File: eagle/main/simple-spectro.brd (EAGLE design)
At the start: 99.1 x 73.7 mm, 46 parts, among them CON1 BAT, CON2 SPI, CON3 SPI, IC1 32U4, IC2 MCP73831T, IC3 MCP1703-33, IC4 DMP1045U, X1 8MHz, X2 MINI-USB

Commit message: add files for new price offer with assembly
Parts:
- C4, C5: value 10µF -> 10u
- R3: value 10K\ -> 10K

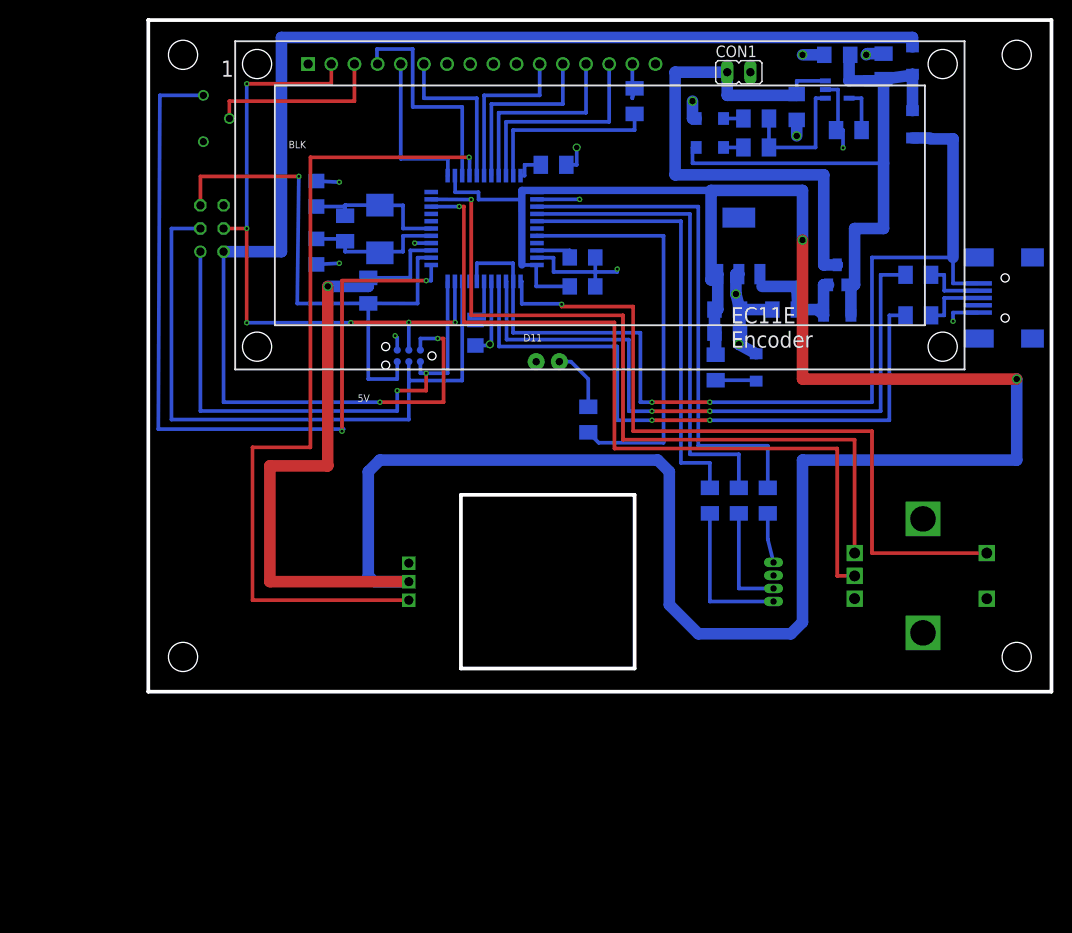
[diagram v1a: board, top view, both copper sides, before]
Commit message: remove right angles
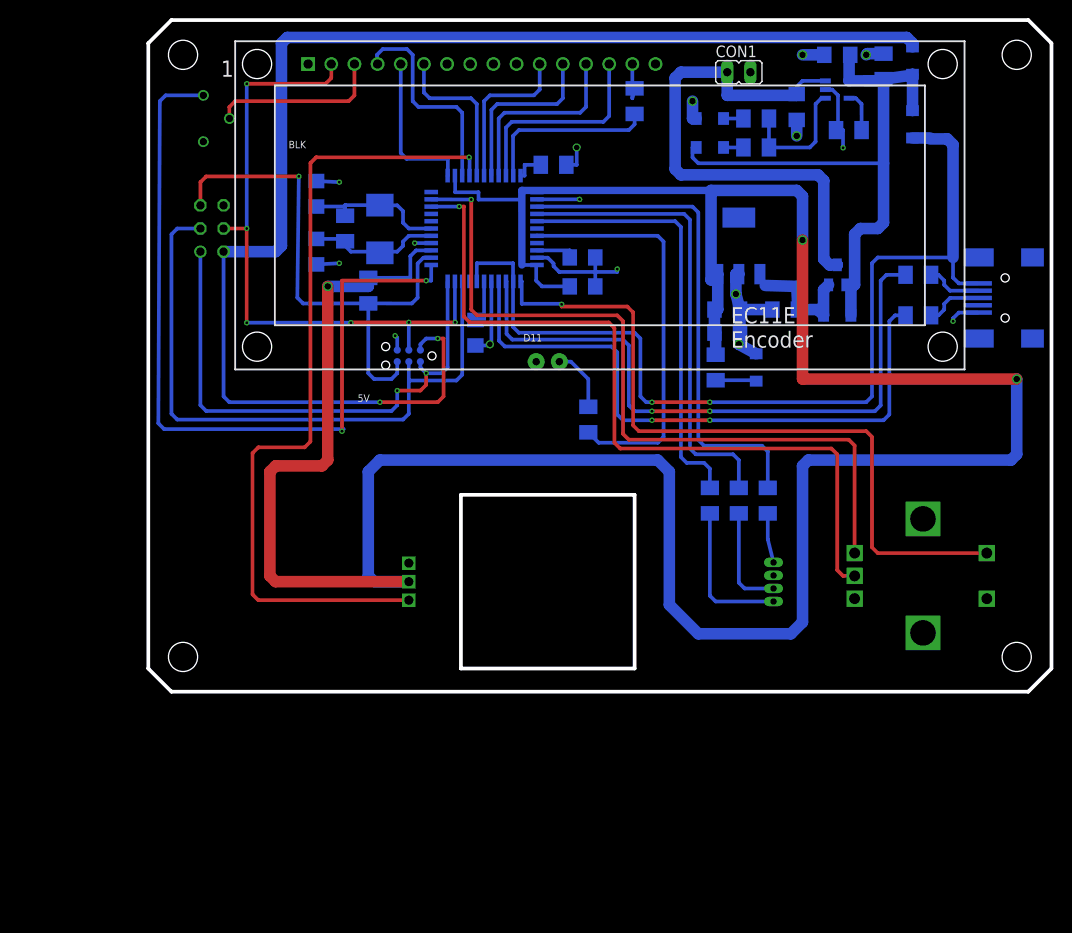
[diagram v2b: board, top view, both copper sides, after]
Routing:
- net VCC: track 332.0 -> 329.0 mm
- net VUSB: track 108.5 -> 105.9 mm
- net RESET: track 61.0 -> 58.8 mm
- net ISP+5V: track 151.5 -> 149.3 mm
- net USB_N: track 73.0 -> 71.2 mm
- net RX: track 87.0 -> 85.1 mm
- net MISO: track 60.7 -> 58.9 mm
- net GND: track 91.9 -> 90.0 mm
- net VBAT1: track 59.7 -> 57.8 mm
- net USB_P: track 71.4 -> 69.5 mm
- net D7*: track 81.2 -> 79.7 mm
- net TX: track 85.2 -> 83.7 mm
- net SCK: track 73.2 -> 71.8 mm
- net A6: track 24.9 -> 23.5 mm
- net D12*: track 91.5 -> 90.1 mm
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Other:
- outline, holes or cut-outs redrawn

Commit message: towards final box
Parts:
- moved R5 1.27 mm to (84.5, 44.5)
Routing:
- net USB_N: track 71.2 -> 69.9 mm
- net USBC_N: track 6.12 -> 5.28 mm

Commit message: update bom
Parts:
- D1, D2, D3: device lpatiny:LED-1206 -> diode:SOD123
- IC4: value DMP1045U -> DMP1045U or DMG2302
- moved D3 0.63 mm to (75.6, 41.9), turned to 180 degrees
- turned D1 to 270 degrees
- turned D2 to 90 degrees
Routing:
- net N$11: track 4.87 -> 2.77 mm
- net VDD: track 14.7 -> 13.4 mm
- net N$15: track 67.9 -> 66.7 mm

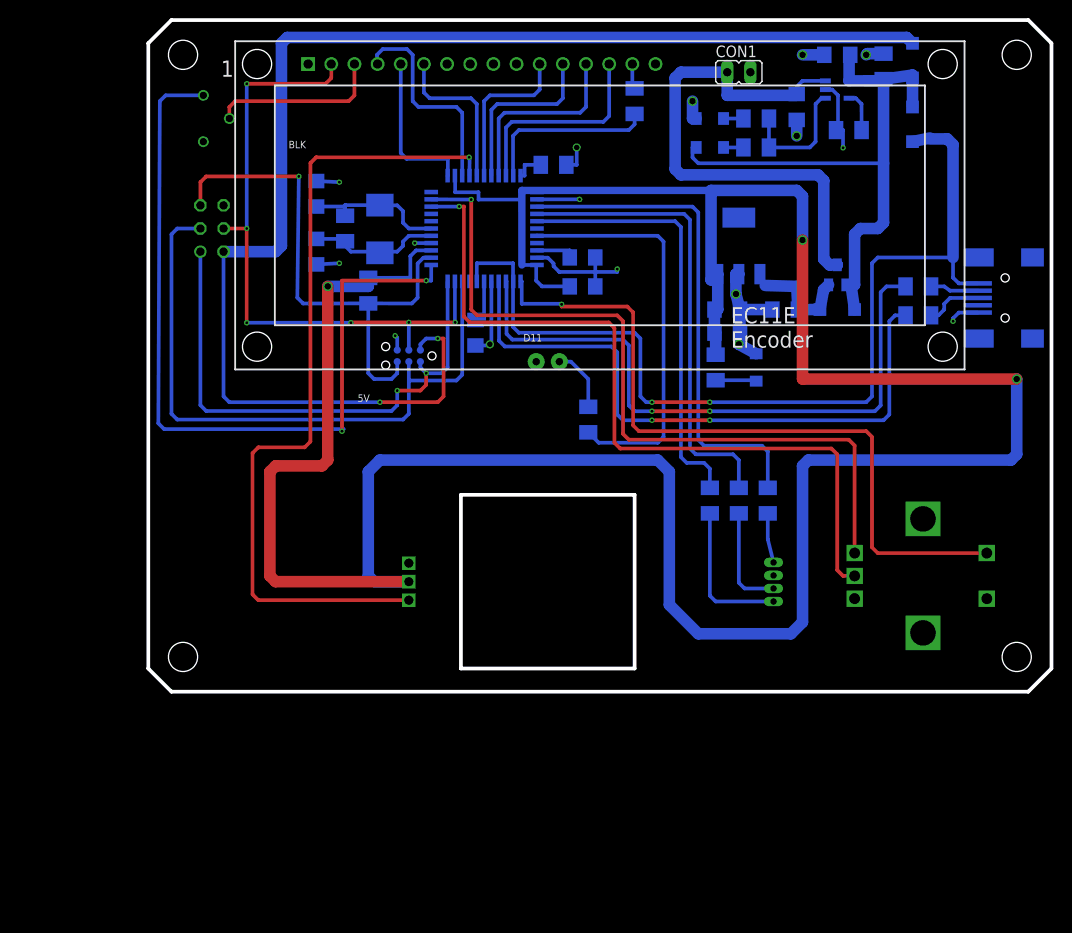
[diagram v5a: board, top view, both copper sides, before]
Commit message: add i2c temperature sensor
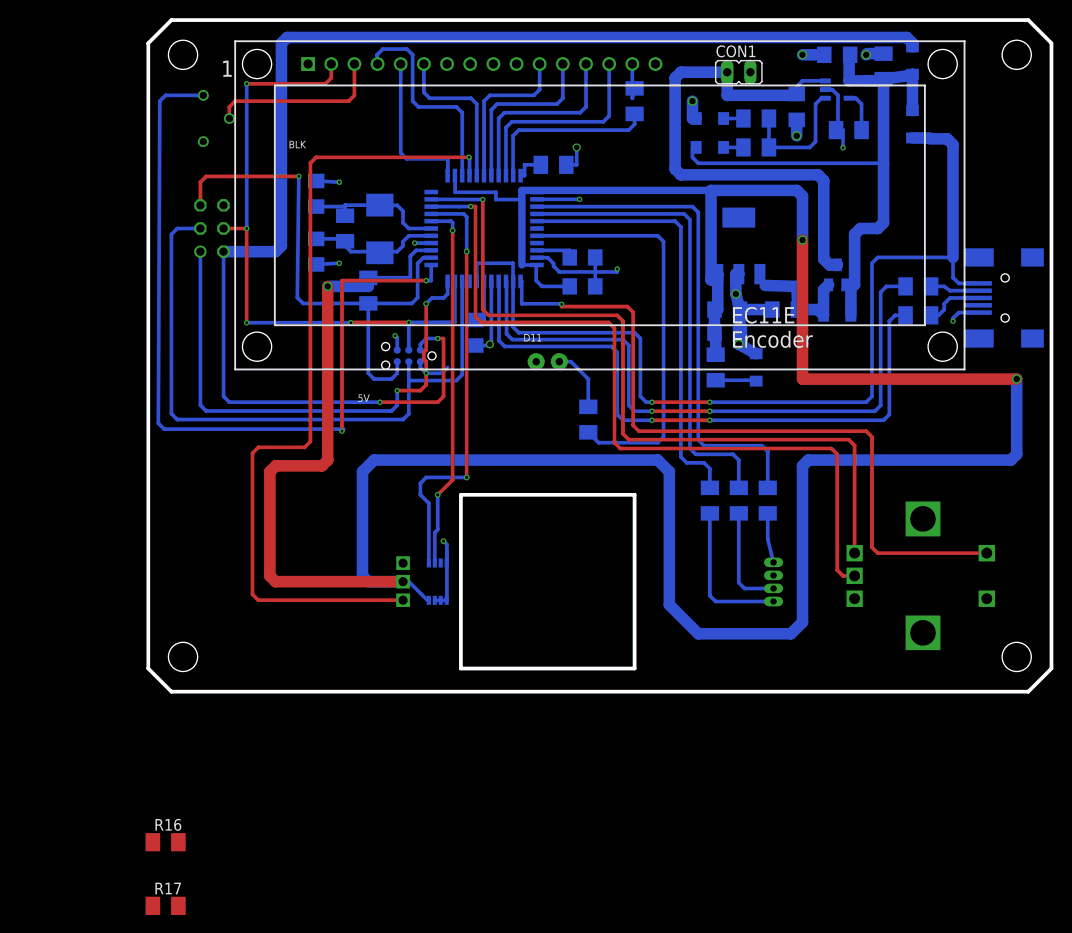
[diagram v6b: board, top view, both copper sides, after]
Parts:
- added R16, R17: 10K, rcl:M1206
- added U1: TMP75DGK, ti_tmp:MSOP8
- D1, D2, D3: device diode:SOD123 -> lpatiny:LED-1206
- IC4: value DMP1045U or DMG2302 -> DMP1045U
- moved U$7 0.64 mm to (25.4, 12.1)
- moved D3 0.63 mm to (75.6, 41.3), turned to 0 degrees
- turned D1 to 90 degrees
- turned D2 to 270 degrees
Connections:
- net GND: now also U1.4, U1.5, U1.6, U1.7
- net SCL: now also R17.1, U1.2
- net SDA: now also R16.1, U1.1
- net VCC: now also R16.2, R17.2, U1.8
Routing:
- net SDA: track 0.00 -> 47.1 mm, vias 0 -> 2
- net SCL: track 0.00 -> 40.6 mm, vias 0 -> 2
- net GND: track 90.0 -> 99.1 mm, vias 16 -> 17
- net VCC: track 329.0 -> 332.7 mm
- net MISO: track 58.9 -> 61.4 mm, vias 2 -> 3
- net N$11: track 2.77 -> 4.87 mm
- net VDD: track 13.4 -> 14.7 mm
- net N$15: track 66.7 -> 67.9 mm
- net D12*: track 90.1 -> 89.4 mm
- net MOSI: track 70.3 -> 70.2 mm, vias 6 -> 5

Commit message: clean up
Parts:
- added R18, R19: 10K, rcl:M1206
- D1, D2, D3: device lpatiny:LED-1206 -> diode:SOD123
- IC4: value DMP1045U -> DMP1045U or DMG2302
- moved R17 52.6 mm to (27.9, 22.2), flipped to the bottom
- moved R16 43.6 mm to (27.9, 18.4), flipped to the bottom
- moved U$7 0.64 mm to (26.0, 12.1)
- moved D3 0.63 mm to (75.6, 41.9), turned to 180 degrees
- turned D1 to 270 degrees
- turned D2 to 90 degrees
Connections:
- net A3: now also R18.1, R19.2
- net GND: now also R19.1
- net VBAT1: now also R18.2
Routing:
- net A3: track 0.00 -> 20.1 mm, vias 0 -> 2
- net GND: track 99.1 -> 93.9 mm, vias 17 -> 16
- net VBAT1: track 57.8 -> 61.1 mm
- net SDA: track 47.1 -> 44.4 mm, vias 2 -> 1
- net SCL: track 40.6 -> 43.0 mm
- net N$11: track 4.87 -> 2.77 mm
- net VDD: track 14.7 -> 13.4 mm
- net N$15: track 67.9 -> 66.7 mm
- net VCC: track 332.7 -> 333.9 mm
- net MISO: track 61.4 -> 62.4 mm, vias 3 -> 2
- net D12*: track 89.4 -> 90.1 mm
- net MOSI: vias 5 -> 6

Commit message: working on vibration
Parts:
- added CON4: VIBR, jumper:JP1
- added R20: 1k, rcl:M1206
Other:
- board text added: "Simple spectro V 1.4.0"
- board text added: "Simple spectro V1.4.0"
- board text removed: "Simple spectro V 1.3.0"
- board text removed: "Simple spectro V1.3.0"
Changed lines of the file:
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@@
 <hole x="95.25" y="3.81" drill="3.2"/>
 <text x="32.385" y="1.905" size="1.778" layer="28" rot="MR0">Simple spectro
-V1.3.0</text>
+V1.4.0</text>
 <text x="55.88" y="1.905" size="1.778" layer="27">Simple spectro
-V 1.3.0</text>
+V 1.4.0</text>
 <wire x1="34.29" y1="21.59" x2="53.34" y2="21.59" width="0.4064" layer="20"/>
 <wire x1="53.34" y1="21.59" x2="53.34" y2="2.54" width="0.4064" layer="20"/>
@@
 <attribute name="VALUE" x="49.53" y="60.6679" size="1.27" layer="28" rot="MR270"/>
 </element>
+<element name="CON4" library="jumper" package="JP1" value="VIBR" x="-8.255" y="-4.445"/>
+<element name="R20" library="rcl" package="M1206" value="1k" x="-12.065" y="-16.51">
+<attribute name="ELECROW" value="C4410" x="-12.065" y="-16.51" size="1.778" layer="27" display="off"/>
+<attribute name="LCSC" value="C1469" x="-12.065" y="-16.51" size="1.778" layer="27" display="off"/>
+<attribute name="MPN" value="667-ERJ-8GEYJ101V" x="-12.065" y="-16.51" size="1.778" layer="27" display="off"/>
+</element>
 </elements>
